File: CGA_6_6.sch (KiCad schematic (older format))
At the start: 89 parts, among them J1 VIDEO JACK, J2 RGBI Output, P1 1X4 BERG, P2 1X6 BERG, P5 Bus_ISA_8bit, U13 74LS08, U14 74LS32, U20 74LS04, U26 74S04, U41 74LS08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

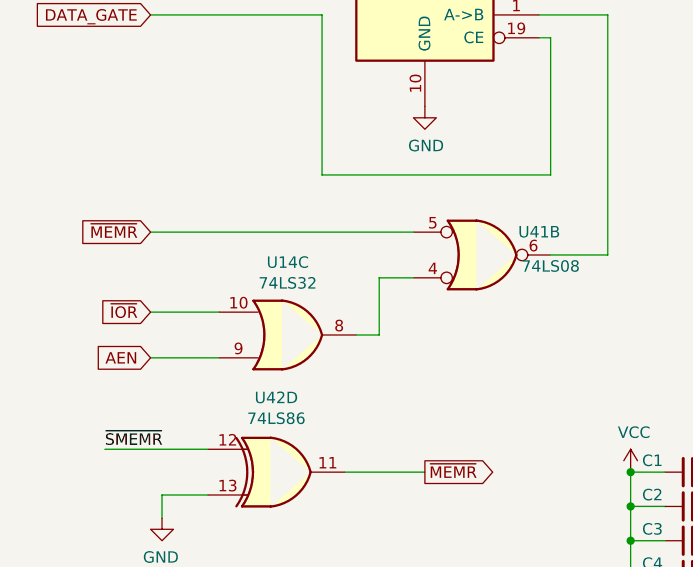
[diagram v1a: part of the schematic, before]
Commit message: Reorganize space between ICs
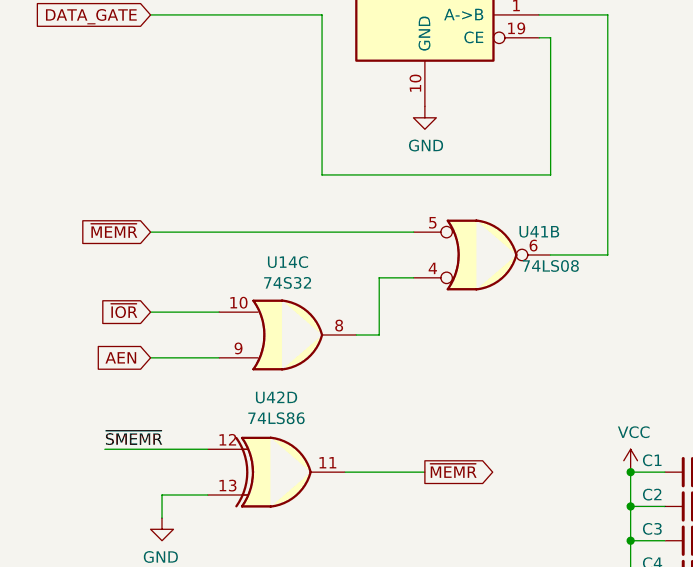
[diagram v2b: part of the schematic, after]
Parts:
- U14: value 74LS32 -> 74S32
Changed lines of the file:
@@
 AR Path="/60463D9E/64CA00B2" Ref="U14"  Part="3"
 F 0 "U14" H 2000 3283 50  0000 C CNN
-F 1 "74LS32" H 2000 3374 50  0000 C CNN
+F 1 "74S32" H 2000 3374 50  0000 C CNN
 F 2 "Package_DIP:DIP-14_W7.62mm_LongPads" H 2000 3600 50  0001 C CNN
 F 3 "http://www.ti.com/lit/gpn/sn74LS32" H 2000 3600 50  0001 C CNN

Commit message: Changed footprints, moving components
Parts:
- U13, U14, U20, U26, U41, U42: footprint Package_DIP:DIP-14_W7.62mm_LongPads -> Package_DIP:DIP-14_W7.62mm
- U66: footprint Package_DIP:DIP-20_W7.62mm_LongPads -> Package_DIP:DIP-20_W7.62mm
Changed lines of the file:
@@
 F 0 "U66" H 2350 2450 50  0000 C CNN
 F 1 "74LS245" H 2850 2450 50  0000 C CNN
-F 2 "Package_DIP:DIP-20_W7.62mm_LongPads" H 2600 1800 50  0001 C CNN
+F 2 "Package_DIP:DIP-20_W7.62mm" H 2600 1800 50  0001 C CNN
 F 3 "http://www.ti.com/lit/gpn/sn74LS245" H 2600 1800 50  0001 C CNN
 	1    2600 1800
@@
 F 0 "U41" H 3100 3150 50  0000 C CNN
 F 1 "74LS08" H 3150 3300 50  0000 C CNN
-F 2 "Package_DIP:DIP-14_W7.62mm_LongPads" H 2850 3250 50  0001 C CNN
+F 2 "Package_DIP:DIP-14_W7.62mm" H 2850 3250 50  0001 C CNN
 F 3 "http://www.ti.com/lit/gpn/sn74LS08" H 2850 3250 50  0001 C CNN
 	2    2850 3250
@@
 F 0 "U14" H 2000 3283 50  0000 C CNN
 F 1 "74S32" H 2000 3374 50  0000 C CNN
-F 2 "Package_DIP:DIP-14_W7.62mm_LongPads" H 2000 3600 50  0001 C CNN
+F 2 "Package_DIP:DIP-14_W7.62mm" H 2000 3600 50  0001 C CNN
 F 3 "http://www.ti.com/lit/gpn/sn74LS32" H 2000 3600 50  0001 C CNN
 	3    2000 3600
@@
 F 0 "U13" H 9900 4033 50  0000 C CNN
 F 1 "74LS08" H 9900 4124 50  0000 C CNN
-F 2 "Package_DIP:DIP-14_W7.62mm_LongPads" H 9900 4350 50  0001 C CNN
+F 2 "Package_DIP:DIP-14_W7.62mm" H 9900 4350 50  0001 C CNN
 F 3 "http://www.ti.com/lit/gpn/sn74LS08" H 9900 4350 50  0001 C CNN
 	2    9900 4350
@@
 F 0 "U20" H 1900 4650 50  0000 C CNN
 F 1 "74LS04" H 1900 4750 50  0000 C CNN
-F 2 "Package_DIP:DIP-14_W7.62mm_LongPads" H 1950 4950 50  0001 C CNN
+F 2 "Package_DIP:DIP-14_W7.62mm" H 1950 4950 50  0001 C CNN
 F 3 "http://www.ti.com/lit/gpn/sn74LS04" H 1950 4950 50  0001 C CNN
 	4    1950 4950
@@
 F 0 "U26" H 1900 5400 50  0000 C CNN
 F 1 "74S04" H 1900 5500 50  0000 C CNN
-F 2 "Package_DIP:DIP-14_W7.62mm_LongPads" H 1950 5700 50  0001 C CNN
+F 2 "Package_DIP:DIP-14_W7.62mm" H 1950 5700 50  0001 C CNN
 F 3 "http://www.ti.com/lit/gpn/sn74LS04" H 1950 5700 50  0001 C CNN
 	6    1950 5700
@@
 F 0 "U42" H 1950 4525 50  0000 C CNN
 F 1 "74LS86" H 1950 4434 50  0000 C CNN
-F 2 "Package_DIP:DIP-14_W7.62mm_LongPads" H 1950 4200 50  0001 C CNN
+F 2 "Package_DIP:DIP-14_W7.62mm" H 1950 4200 50  0001 C CNN
 F 3 "74xx/74ls86.pdf" H 1950 4200 50  0001 C CNN
 	4    1950 4200

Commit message: Replaced RCA jack
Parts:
- J1: footprint w_conn_av:rca_yellow -> My_Components:Conn_RCA_Right
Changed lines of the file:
@@
 F 0 "J1" H 5050 1025 50  0000 L CNN
 F 1 "VIDEO JACK" H 5050 934 50  0000 L CNN
-F 2 "w_conn_av:rca_yellow" H 4950 1050 50  0001 C CNN
+F 2 "My_Components:Conn_RCA_Right" H 4950 1050 50  0001 C CNN
 F 3 " ~" H 4950 1050 50  0001 C CNN
 	1    4950 1050

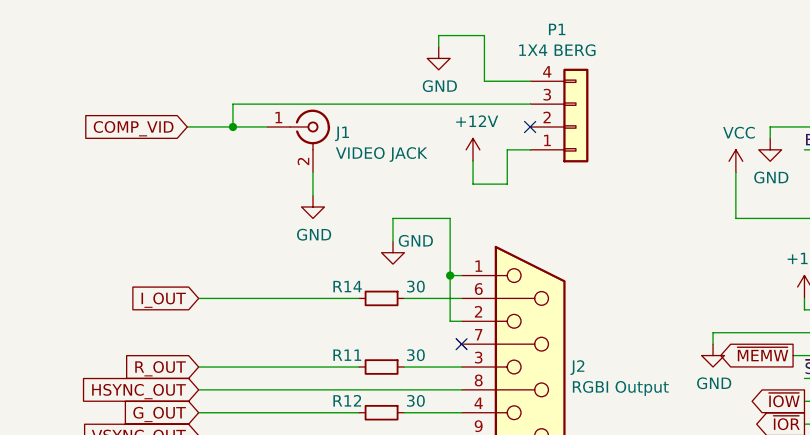
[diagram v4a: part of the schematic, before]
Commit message: Renamed components, cleaned the silkscreen
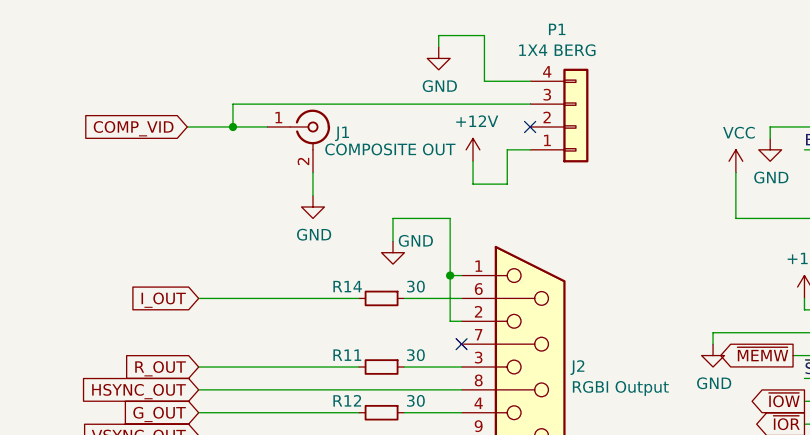
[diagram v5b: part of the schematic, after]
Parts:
- J1: value VIDEO JACK -> COMPOSITE OUT
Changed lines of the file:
@@
 P 4950 1050
 F 0 "J1" H 5050 1025 50  0000 L CNN
-F 1 "VIDEO JACK" H 5050 934 50  0000 L CNN
+F 1 "COMPOSITE OUT" H 5000 950 50  0000 L CNN
 F 2 "My_Components:Conn_RCA_Right" H 4950 1050 50  0001 C CNN
 F 3 " ~" H 4950 1050 50  0001 C CNN
